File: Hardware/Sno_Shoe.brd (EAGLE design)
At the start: 20.3 x 57.1 mm, 47 parts, among them J1 QWIIC_RIGHT_ANGLE, J2 MOLEX_HDMI_208658-1051, U1 CH340E

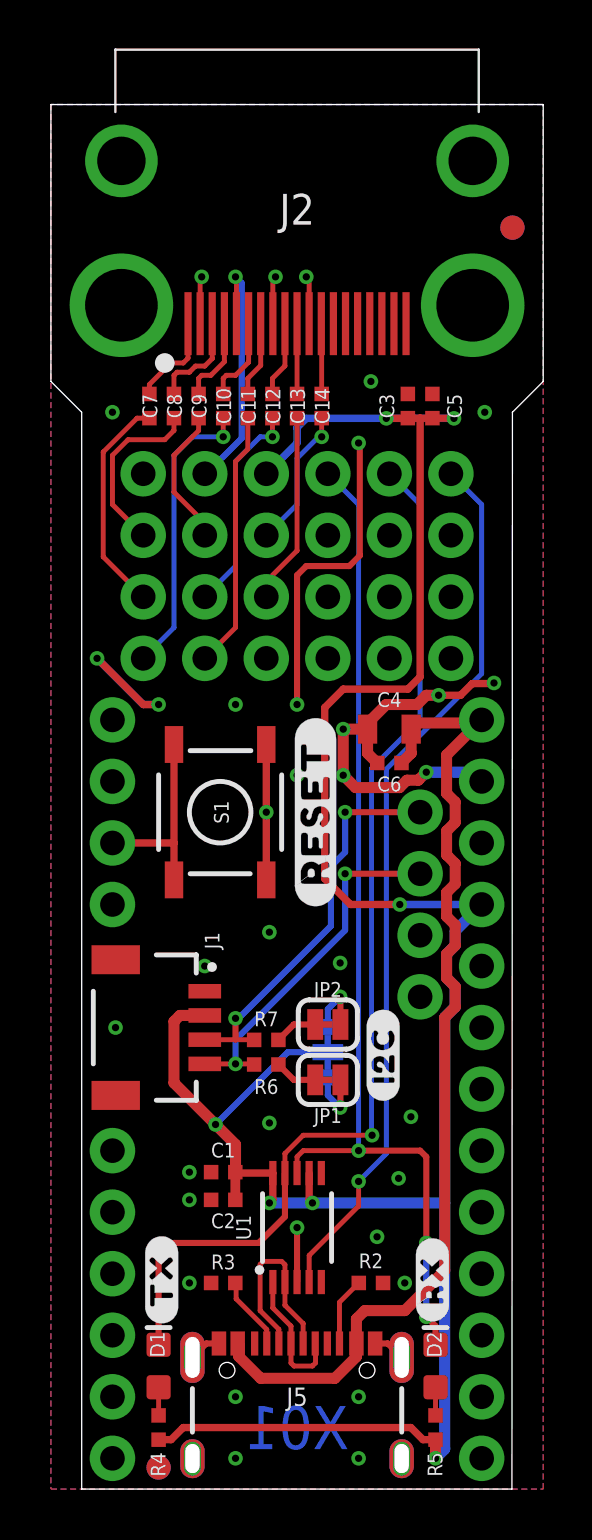
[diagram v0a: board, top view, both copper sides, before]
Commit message: Changed the HDMI connector footprint
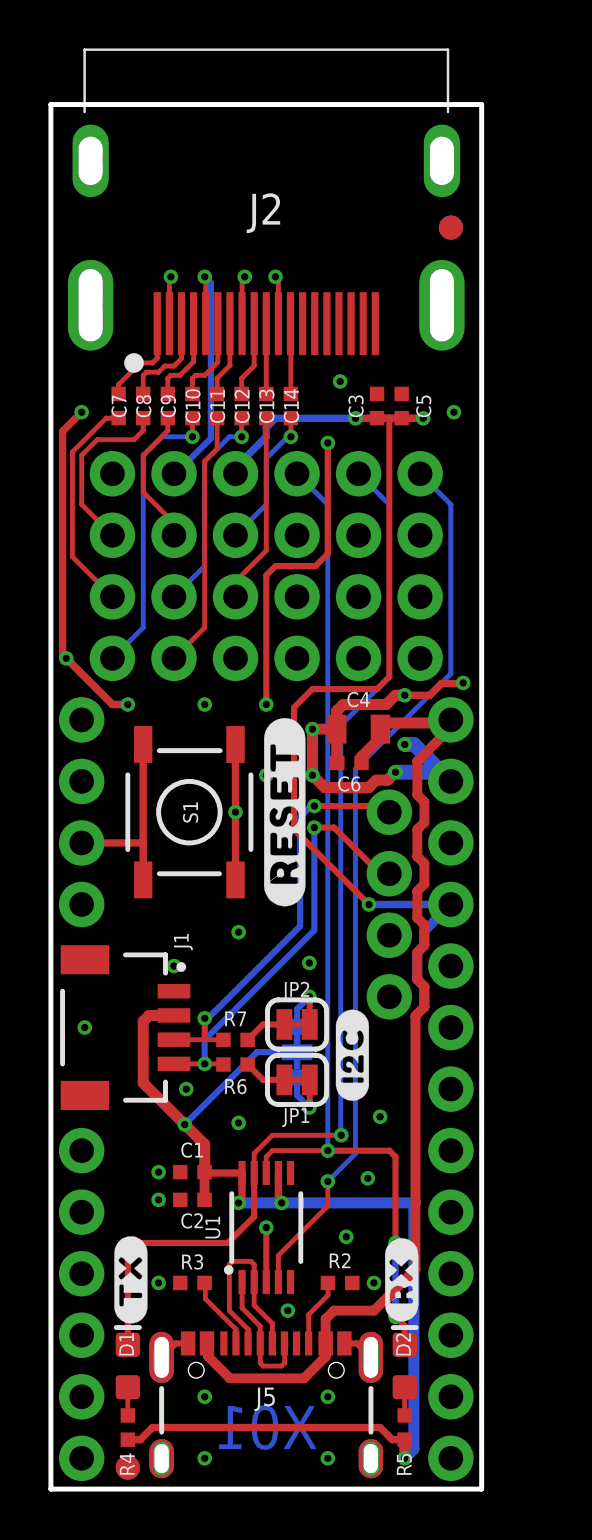
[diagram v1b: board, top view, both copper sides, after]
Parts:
- moved FRAME1 128.3 mm to (48.3, 54.6)
- moved LOGO1 128.3 mm to (22.9, 50.8)
- moved FD1 2.54 mm to (16.5, 52.1)
- moved FD3 2.54 mm to (16.5, 52.1)
- moved C6 1.65 mm to (12.3, 30.0)
- moved C4 1.27 mm to (12.7, 31.4)
- moved U$5 1.27 mm to (9.65, 27.9)
- moved C1 1.27 mm to (5.84, 13.1)
- moved C10 1.27 mm to (5.84, 44.7)
- moved C11 1.27 mm to (6.86, 44.7)
- moved C12 1.27 mm to (7.87, 44.7)
- moved C2 1.27 mm to (5.84, 11.9)
- moved C9 1.27 mm to (4.83, 44.7)
- moved D1 1.27 mm to (3.17, 5.08)
- moved FD2 1.27 mm to (3.17, 0.89)
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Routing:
- net GND: track 63.8 -> 76.9 mm, vias 36 -> 39
- net SCL: track 14.9 -> 17.6 mm
- net 3.3V: track 104.6 -> 103.4 mm
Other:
- board size 20.3 x 57.1 mm -> 17.8 x 57.1 mm
